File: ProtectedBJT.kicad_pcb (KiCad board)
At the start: 2 copper layers, 38.6 x 40.1 mm, 37 parts, among them P1 CONN_01X04, Q1 BC856, Q2 BC850, Q3 BC856, Q4 BC850, Q5 BC856, Q6 BC850, Q7 BD237, Q8 BD250A

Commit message: some changes on board
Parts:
- moved R10 1.87 mm to (137.2, 113.3)
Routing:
- net Net-(C2-Pad1): track 21.6 -> 24.6 mm
- net GND: track 56.6 -> 58.7 mm
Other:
- board text added: "08/2017 - Protected BJT - V. 0.2 Stefan Helmert - entroserv.de"
- board text removed: "08/2017 - Protected BJT - V. 0.1 Stefan Helmert - entroserv.de"
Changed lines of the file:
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@@
   (general
     (links 54)
-    (no_connects 1)
+    (no_connects 0)
     (area 122.104999 96.21 175.513 144.347001)
     (thickness 1.6)
     (drawings 7)
-    (tracks 200)
+    (tracks 205)
     (zones 0)
     (modules 37)
@@
   )
   (module Resistors_SMD:R_1206 (layer F.Cu)
-    (at 138.115 114.935 180)
+    (at 137.234 113.284 180)
     (descr "Resistor SMD 1206, reflow soldering, Vishay (see dcrcw.pdf)")
     (tags "resistor 1206")
@@
     )
   )
-  (gr_text "08/2017 - Protected BJT - V. 0.1\nStefan Helmert - entroserv.de" (at 144.272 134.62) (layer B.SilkS)
+  (gr_text "08/2017 - Protected BJT - V. 0.2\nStefan Helmert - entroserv.de" (at 144.272 134.62) (layer B.SilkS)
     (effects (font (size 1 1) (thickness 0.2)) (justify mirror))
   )
@@
   (segment (start 148.59 138.31024) (end 148.59 136.96988) (width 0.5) (layer F.Cu) (net 11))
   (segment (start 149.03488 136.525) (end 150.18512 136.525) (width 0.5) (layer F.Cu) (net 11))
+  (segment (start 139.065 116.332) (end 139.065 124.06973) (width 0.5) (layer F.Cu) (net 12))
+  (segment (start 140.335 114.935) (end 139.485 114.935) (width 0.5) (layer F.Cu) (net 12))
+  (segment (start 139.485 114.935) (end 139.065 115.355) (width 0.5) (layer F.Cu) (net 12))
+  (segment (start 139.065 115.355) (end 139.065 116.332) (width 0.5) (layer F.Cu) (net 12))
+  (segment (start 140.335 114.935) (end 138.684 113.284) (width 0.5) (layer F.Cu) (net 12))
   (segment (start 146.05 124.46) (end 146.05 125.735) (width 0.5) (layer F.Cu) (net 12))
   (segment (start 146.05 125.735) (end 142.88 125.735) (width 0.5) (layer F.Cu) (net 12))
@@
   (segment (start 146.685 136.525) (end 146.685 135.25) (width 0.5) (layer F.Cu) (net 12))
   (segment (start 146.685 135.25) (end 146.05 134.615) (width 0.5) (layer F.Cu) (net 12))
-  (segment (start 139.065 114.935) (end 139.065 124.06973) (width 0.5) (layer F.Cu) (net 12))
   (segment (start 139.065 124.06973) (end 139.45527 124.46) (width 0.5) (layer F.Cu) (net 12))
   (segment (start 139.45527 124.46) (end 141.605 124.46) (width 0.5) (layer F.Cu) (net 12))
-  (segment (start 140.335 114.935) (end 139.065 114.935) (width 0.5) (layer F.Cu) (net 12))
   (segment (start 140.97 123.825) (end 141.605 124.46) (width 0.5) (layer F.Cu) (net 12))
   (segment (start 141.605 124.46) (end 139.7 124.46) (width 0.5) (layer F.Cu) (net 12))
@@
   (segment (start 153.67 133.985) (end 151.86 133.985) (width 0.5) (layer F.Cu) (net 18))
   (segment (start 151.86 133.985) (end 151.765 134.08) (width 0.5) (layer F.Cu) (net 18))
+  (segment (start 135.784 113.284) (end 134.14794 113.284) (width 0.5) (layer F.Cu) (net 19))
+  (segment (start 134.14794 113.284) (end 133.35 114.08194) (width 0.5) (layer F.Cu) (net 19))
+  (segment (start 133.35 114.08194) (end 133.35 116.332) (width 0.5) (layer F.Cu) (net 19))
   (segment (start 133.35 116.332) (end 135.768 116.332) (width 0.5) (layer F.Cu) (net 19))
-  (segment (start 135.768 116.332) (end 137.165 114.935) (width 0.5) (layer F.Cu) (net 19))
   (segment (start 132.34924 116.332) (end 133.35 116.332) (width 0.5) (layer F.Cu) (net 19))
   (segment (start 134.372 116.332) (end 133.35 116.332) (width 0.5) (layer F.Cu) (net 19))

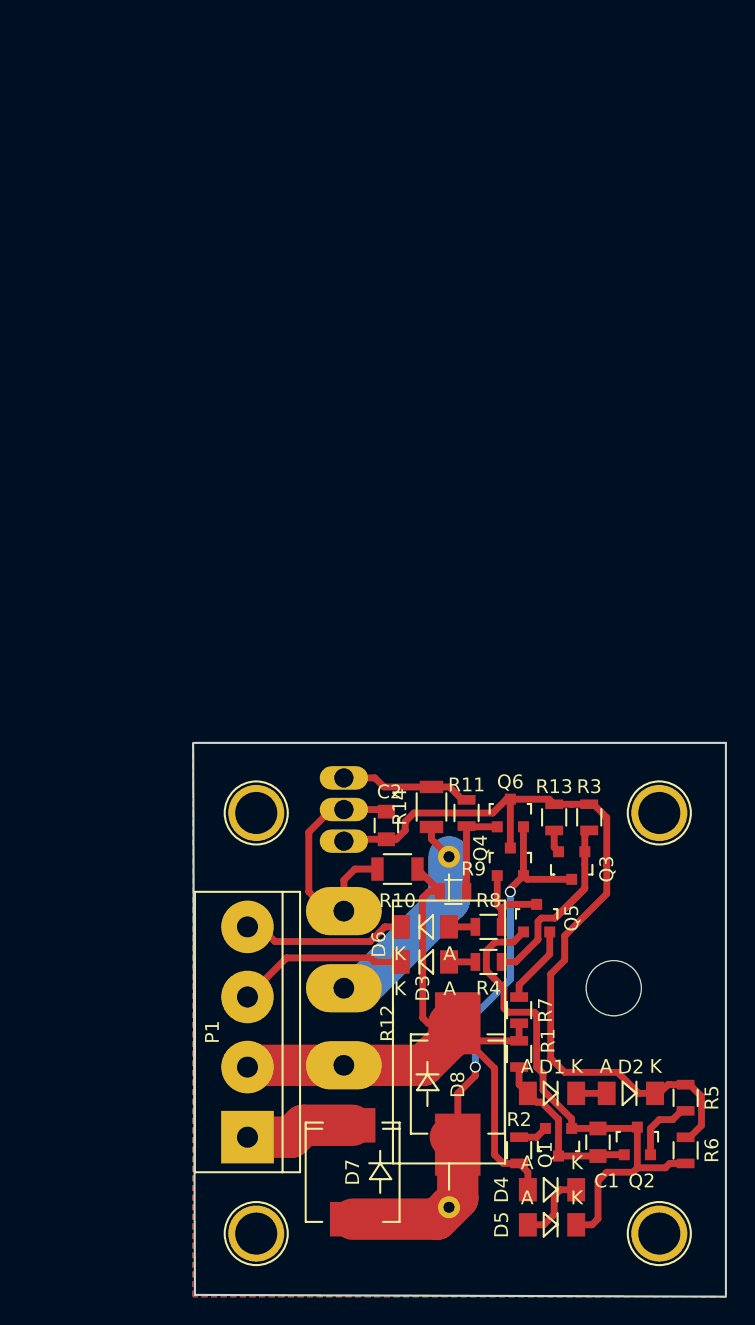
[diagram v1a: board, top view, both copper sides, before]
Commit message: completely new version wth darlington output transistor
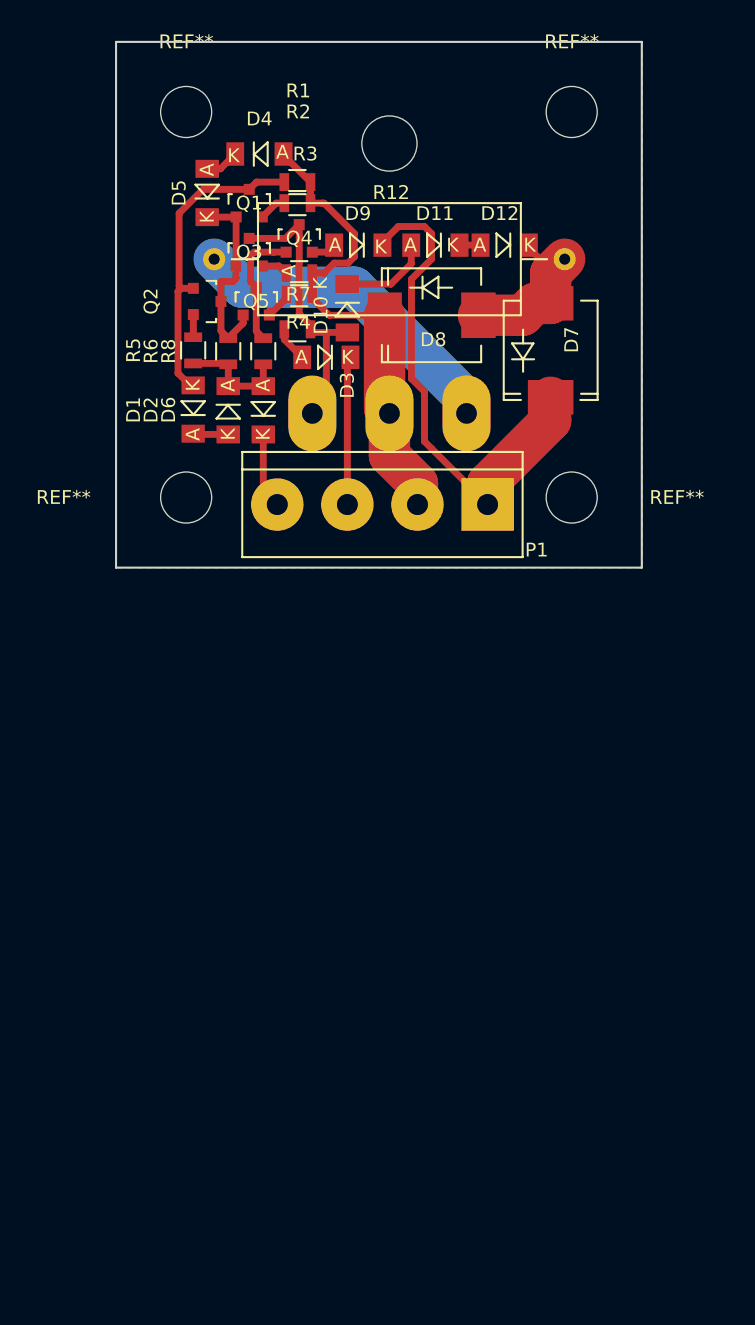
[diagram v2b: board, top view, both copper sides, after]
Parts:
- removed C1, C2: 1p, Capacitors_SMD:C_0805
- removed Q7: BD237, TO_SOT_Packages_THT:SOT126_SOT32_Housing_Vertical_BigPads
- removed Q8: BD250A, TO_SOT_Packages_THT:TO-247_Horizontal_Neutral123_Reverse_largePads
- removed R10: 100, Resistors_SMD:R_1206
- removed R11: 10k, Resistors_SMD:R_0805
- removed R13: 470, Resistors_SMD:R_0805
- removed R14: 2, Resistors_SMD:R_1206
- removed R9: 1M, Resistors_SMD:R_0805
- removed the REF** at (156.2, 139.7)
- removed the REF** at (156.2, 109.2)
- removed the REF** at (127.0, 139.7)
- removed the REF** at (127.0, 109.2)
- added D10: 1N4148, Diodes_SMD:MiniMELF_Standard, F.Cu at (133.6, 72.6)
- added D11: 1N4148, Diodes_SMD:MiniMELF_Standard, F.Cu at (140.0, 68.1)
- added D12: 1N4148, Diodes_SMD:MiniMELF_Standard, F.Cu at (145.0, 68.1)
- added D9: 1N4148, Diodes_SMD:MiniMELF_Standard, F.Cu at (134.4, 68.1)
- added REF**: MountingHole_3-7mm, Mounting_Holes:MountingHole_3-7mm, F.Cu at (121.9, 58.4)
- added REF**: MountingHole_3-7mm, Mounting_Holes:MountingHole_3-7mm, F.Cu at (149.9, 58.4)
- added REF**: MountingHole_3-7mm, Mounting_Holes:MountingHole_3-7mm, F.Cu at (121.9, 86.4)
- added REF**: MountingHole_3-7mm, Mounting_Holes:MountingHole_3-7mm, F.Cu at (149.9, 86.4)
- D8: footprint Diodes_SMD:SMC_Handsoldering -> Diodes_SMD:SMC_Standard
- Q6: value BC850 -> TIP141; footprint TO_SOT_Packages_SMD:SOT-23 -> TO_SOT_Packages_THT:TO-247_Horizontal_Neutral123_Reverse_largePads; moved to B.Cu
- R3: value 1k -> 47
- R4: value 470 -> 47
- R7, R8: value 10k -> 100
- moved D5 78.8 mm to (123.4, 64.3), turned to 90 degrees
- moved D4 78.0 mm to (127.2, 61.5), turned to 0 degrees
- moved Q1 71.7 mm to (126.5, 65.0), turned to 0 degrees
- moved R2 70.5 mm to (130.0, 65.0), turned to 180 degrees
- moved Q2 68.4 mm to (123.4, 72.2), turned to 270 degrees
- moved R6 66.7 mm to (125.0, 75.8), turned to 270 degrees
- moved R1 65.2 mm to (130.0, 63.5), turned to 180 degrees
- moved R5 64.9 mm to (122.4, 75.7), turned to 270 degrees
- moved D7 61.3 mm to (148.3, 75.7), turned to 90 degrees
- moved D2 57.5 mm to (125.0, 80.0), turned to 270 degrees
- moved R12 56.2 mm to (136.7, 69.1), turned to 0 degrees
- moved D1 56.0 mm to (122.4, 80.0), turned to 90 degrees
- moved D8 55.7 mm to (139.7, 73.2), turned to 0 degrees
- moved R7 54.3 mm to (130.1, 71.6), turned to 180 degrees
- moved Q3 50.2 mm to (126.5, 68.6), turned to 0 degrees
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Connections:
- D2 pad 1: Net-(C2-Pad2) -> Net-(D2-Pad1)
- D4 pad 2: GND -> Net-(D4-Pad2)
- D5 pad 1: Net-(C1-Pad1) -> Net-(D5-Pad1)
- D6 pad 1: Net-(D6-Pad1) -> GND
- D6 pad 2: Net-(D6-Pad2) -> Net-(D2-Pad1)
- D7 pad 2: Net-(D7-Pad2) -> Net-(D12-Pad1)
- D8 pad 1: GND -> Net-(D4-Pad2)
- D8 pad 2: Net-(D7-Pad2) -> Net-(D12-Pad1)
- P1 pad 2: GND -> Net-(D4-Pad2)
- P1 pad 4: Net-(D6-Pad1) -> GND
- Q1 pad 1: Net-(C1-Pad1) -> Net-(D5-Pad1)
- Q2 pad 3: Net-(C1-Pad1) -> Net-(D5-Pad1)
- Q3 pad 1: Net-(Q3-Pad1) -> Net-(D5-Pad1)
- Q3 pad 3: Net-(D7-Pad2) -> Net-(D10-Pad2)
- Q4 pad 2: Net-(D7-Pad2) -> Net-(D9-Pad2)
- Q4 pad 3: Net-(C2-Pad2) -> Net-(D10-Pad2)
- Q5 pad 1: Net-(C1-Pad1) -> Net-(D5-Pad1)
- Q6 pad 1: Net-(Q6-Pad1) -> Net-(D10-Pad2)
- Q6 pad 2: Net-(D7-Pad2) -> Net-(D4-Pad2)
- Q6 pad 3: Net-(C2-Pad2) -> Net-(Q6-Pad3)
- R1 pad 1: GND -> Net-(D4-Pad2)
- R12 pad 1: Net-(Q8-Pad2) -> Net-(Q6-Pad3)
- R12 pad 2: Net-(D7-Pad2) -> Net-(D12-Pad1)
- R2 pad 1: GND -> Net-(D4-Pad2)
- R3 pad 1: Net-(C2-Pad2) -> Net-(D4-Pad2)
- R3 pad 2: Net-(Q3-Pad1) -> Net-(Q3-Pad2)
- R4 pad 1: Net-(Q3-Pad1) -> Net-(D10-Pad2)
- R5 pad 2: Net-(C2-Pad2) -> Net-(D2-Pad1)
- R6 pad 1: Net-(C1-Pad1) -> Net-(D5-Pad1)
- R6 pad 2: Net-(C2-Pad2) -> Net-(D2-Pad1)
- R7 pad 1: GND -> Net-(D4-Pad2)
- R8 pad 2: Net-(D6-Pad2) -> Net-(D2-Pad1)
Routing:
- net Net-(C2-Pad2): track 61.6 -> 0.00 mm
- net GND: track 58.7 -> 5.50 mm
- net (no net): track 43.2 -> 0.00 mm
- net Net-(D7-Pad2): track 41.5 -> 0.00 mm, vias 2 -> 0
- net Net-(C1-Pad1): track 39.2 -> 0.00 mm
- net Net-(D4-Pad2): track 0.00 -> 36.0 mm
- net Net-(D7-Pad1): track 7.98 -> 36.6 mm
- net Net-(C2-Pad1): track 24.6 -> 0.00 mm
- net Net-(Q6-Pad3): track 0.00 -> 23.5 mm
- net Net-(D10-Pad2): track 0.00 -> 22.9 mm
- net Net-(Q3-Pad1): track 16.4 -> 0.00 mm
- net Net-(Q8-Pad2): track 16.2 -> 0.00 mm
- net Net-(D5-Pad1): track 0.00 -> 14.5 mm
- net Net-(D12-Pad1): track 0.00 -> 12.9 mm
- net Net-(D6-Pad1): track 12.0 -> 0.00 mm
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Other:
- board size 38.6 x 40.1 mm -> 38.1 x 38.1 mm
- board text removed: "08/2017 - Protected BJT - V. 0.2 Stefan Helmert - entroserv.de"

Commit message: silk screen ready
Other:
- board text added: "B"
- board text added: "C"
- board text added: "E"
- board text added: "Protected Darl. BJT - V. 0.13 (C) 09/2017 Stefan Helmert entroserv.de"
- board text added: "T"
- board text added: "[ ] NPN [ ] PNP"
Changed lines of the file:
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@@
     (area 116.764999 53.264999 155.015001 91.515001)
     (thickness 1.6)
-    (drawings 6)
+    (drawings 18)
     (tracks 123)
     (zones 0)
@@
     (descr "Mounting hole, Befestigungsbohrung, 3,7mm, No Annular, Kein Restring,")
     (tags "Mounting hole, Befestigungsbohrung, 3,7mm, No Annular, Kein Restring,")
-    (fp_text reference REF** (at 0 -5.08) (layer F.SilkS)
+    (fp_text reference REF** (at -7.366 0.254) (layer F.SilkS)
       (effects (font (size 1 1) (thickness 0.15)))
     )
@@
     (descr "Mounting hole, Befestigungsbohrung, 3,7mm, No Annular, Kein Restring,")
     (tags "Mounting hole, Befestigungsbohrung, 3,7mm, No Annular, Kein Restring,")
-    (fp_text reference REF** (at 0 -5.08) (layer F.SilkS)
+    (fp_text reference REF** (at 6.985 0) (layer F.SilkS)
       (effects (font (size 1 1) (thickness 0.15)))
     )
@@
     (descr "Mounting hole, Befestigungsbohrung, 3,7mm, No Annular, Kein Restring,")
     (tags "Mounting hole, Befestigungsbohrung, 3,7mm, No Annular, Kein Restring,")
-    (fp_text reference REF** (at -8.89 0) (layer F.SilkS)
+    (fp_text reference REF** (at -7.112 0.127) (layer F.SilkS)
       (effects (font (size 1 1) (thickness 0.15)))
     )
@@
     (descr "Bornier d'alimentation 4 pins")
     (tags DEV)
-    (fp_text reference P1 (at -11.176 -3.302 180) (layer F.SilkS)
+    (fp_text reference P1 (at -9.271 4.445 180) (layer F.SilkS)
       (effects (font (size 1 1) (thickness 0.15)))
     )
@@
     (tags "Diode Mini-MELF Standard")
     (attr smd)
-    (fp_text reference D3 (at -1.524 -2.032 270) (layer F.SilkS)
+    (fp_text reference D3 (at 0 13.97 360) (layer F.SilkS)
       (effects (font (size 1 1) (thickness 0.15)))
     )
@@
     (tags "Diode Mini-MELF Standard")
     (attr smd)
-    (fp_text reference D4 (at 0 -2.54) (layer F.SilkS)
+    (fp_text reference D4 (at 0.02794 -6.223) (layer F.SilkS)
       (effects (font (size 1 1) (thickness 0.15)))
     )
@@
     (tags "Diode SMC Standard")
     (attr smd)
-    (fp_text reference D7 (at 0.762 1.524 90) (layer F.SilkS)
+    (fp_text reference D7 (at 0.127 4.191 90) (layer F.SilkS)
       (effects (font (size 1 1) (thickness 0.15)))
     )
@@
     (tags "Diode Mini-MELF Standard")
     (attr smd)
-    (fp_text reference D10 (at 0.508 1.905 450) (layer F.SilkS)
+    (fp_text reference D10 (at -0.381 12.446 450) (layer F.SilkS)
       (effects (font (size 1 1) (thickness 0.15)))
     )
@@
     (fp_line (start 0.60052 0.85) (end -0.40024 0) (layer F.SilkS) (width 0.15))
     (fp_line (start -0.40024 -0.85) (end -0.40024 0.85) (layer F.SilkS) (width 0.15))
-    (fp_text user K (at -1.8 1.95 270) (layer F.SilkS)
-      (effects (font (size 1 1) (thickness 0.15)))
-    )
-    (fp_text user A (at -2.7051 4.2164 270) (layer F.SilkS)
+    (fp_text user K (at -1.905 0 270) (layer F.SilkS)
+      (effects (font (size 1 1) (thickness 0.15)))
+    )
+    (fp_text user A (at 1.651 0 270) (layer F.SilkS)
       (effects (font (size 1 1) (thickness 0.15)))
     )
@@
     (fp_line (start 0.60052 0.85) (end -0.40024 0) (layer F.SilkS) (width 0.15))
     (fp_line (start -0.40024 -0.85) (end -0.40024 0.85) (layer F.SilkS) (width 0.15))
-    (fp_text user K (at -1.24206 0 180) (layer F.SilkS)
+    (fp_text user K (at -1.87706 0 180) (layer F.SilkS)
       (effects (font (size 1 1) (thickness 0.15)))
     )
@@
     (tags SOT-23)
     (attr smd)
-    (fp_text reference Q1 (at 0 0) (layer F.SilkS)
+    (fp_text reference Q1 (at -0.254 -8.382) (layer F.SilkS)
       (effects (font (size 1 1) (thickness 0.15)))
     )
@@
     (tags SOT-23)
     (attr smd)
-    (fp_text reference Q3 (at 0 0) (layer F.SilkS)
+    (fp_text reference Q3 (at -0.381 -10.541) (layer F.SilkS)
       (effects (font (size 1 1) (thickness 0.15)))
     )
@@
     (tags SOT-23)
     (attr smd)
-    (fp_text reference Q4 (at 0 -0.01524) (layer F.SilkS)
+    (fp_text reference Q4 (at -0.32 -10.30224) (layer F.SilkS)
       (effects (font (size 1 1) (thickness 0.15)))
     )
@@
     (tags SOT-23)
     (attr smd)
-    (fp_text reference Q5 (at 0 0) (layer F.SilkS)
+    (fp_text reference Q5 (at -0.127 -12.573) (layer F.SilkS)
       (effects (font (size 1 1) (thickness 0.15)))
     )
@@
     (tags "resistor 0805")
     (attr smd)
-    (fp_text reference R1 (at -0.066 6.604 180) (layer F.SilkS)
+    (fp_text reference R1 (at 0.188 8.763 360) (layer F.SilkS)
       (effects (font (size 1 1) (thickness 0.15)))
     )
@@
     (tags "resistor 0805")
     (attr smd)
-    (fp_text reference R2 (at -0.066 6.604 180) (layer F.SilkS)
+    (fp_text reference R2 (at 0.188 9.017 360) (layer F.SilkS)
       (effects (font (size 1 1) (thickness 0.15)))
     )
@@
     (tags "resistor 0805")
     (attr smd)
-    (fp_text reference R3 (at -0.442 8.636 180) (layer F.SilkS)
+    (fp_text reference R3 (at 0.32 11.557 360) (layer F.SilkS)
       (effects (font (size 1 1) (thickness 0.15)))
     )
@@
     (tags "resistor 0805")
     (attr smd)
-    (fp_text reference R4 (at -0.066 0.508 180) (layer F.SilkS)
+    (fp_text reference R4 (at -0.701 13.081 360) (layer F.SilkS)
       (effects (font (size 1 1) (thickness 0.15)))
     )
@@
     (tags "resistor 0805")
     (attr smd)
-    (fp_text reference R7 (at 0.066 0 180) (layer F.SilkS)
+    (fp_text reference R7 (at 0.32 11.811 360) (layer F.SilkS)
       (effects (font (size 1 1) (thickness 0.15)))
     )
@@
     (tags "Diode SMC Standard")
     (attr smd)
-    (fp_text reference D8 (at 0.127 1.778) (layer F.SilkS)
+    (fp_text reference D8 (at -0.127 4.064) (layer F.SilkS)
       (effects (font (size 1 1) (thickness 0.15)))
     )
@@
     (descr "Mounting hole, Befestigungsbohrung, 3,7mm, No Annular, Kein Restring,")
     (tags "Mounting hole, Befestigungsbohrung, 3,7mm, No Annular, Kein Restring,")
-    (fp_text reference REF** (at 7.62 0) (layer F.SilkS)
+    (fp_text reference REF** (at 6.858 0.508) (layer F.SilkS)
       (effects (font (size 1 1) (thickness 0.15)))
     )
@@
     (pad 1 thru_hole circle (at 0 0) (size 3.7 3.7) (drill 3.7) (layers))
   )
+  (gr_text "[ ] NPN\n[ ] PNP" (at 143.51 61.976) (layer F.SilkS)
+    (effects (font (size 1.5 1.5) (thickness 0.3)))
+  )
+  (gr_text "[ ] NPN\n[ ] PNP" (at 149.606 73.66) (layer B.SilkS)
+    (effects (font (size 1.5 1.5) (thickness 0.3)) (justify mirror))
+  )
+  (gr_text "Protected Darl. BJT - V. 0.13\n(C) 09/2017 Stefan Helmert\n    entroserv.de" (at 119.888 61.849 90) (layer B.SilkS)
+    (effects (font (size 0.75 0.75) (thickness 0.15)) (justify left mirror))
+  )
+  (gr_text "Protected Darl. BJT - V. 0.13\n(C) 09/2017 Stefan Helmert\n    entroserv.de" (at 131.191 56.007) (layer F.SilkS)
+    (effects (font (size 0.75 0.75) (thickness 0.15)) (justify left))
+  )
+  (gr_text E (at 146.939 89.662) (layer B.SilkS)
+    (effects (font (size 1.5 1.5) (thickness 0.3)) (justify mirror))
+  )
+  (gr_text C (at 140.716 89.789) (layer B.SilkS)
+    (effects (font (size 1.5 1.5) (thickness 0.3)) (justify mirror))
+  )
+  (gr_text B (at 135.89 89.662) (layer B.SilkS)
+    (effects (font (size 1.5 1.5) (thickness 0.3)) (justify mirror))
+  )
+  (gr_text T (at 130.937 89.408 180) (layer B.SilkS)
+    (effects (font (size 1.5 1.5) (thickness 0.3)) (justify mirror))
+  )
+  (gr_text E (at 146.939 89.789) (layer F.SilkS)
+    (effects (font (size 1.5 1.5) (thickness 0.3)))
+  )
+  (gr_text C (at 140.589 89.662) (layer F.SilkS)
+    (effects (font (size 1.5 1.5) (thickness 0.3)))
+  )
+  (gr_text "B\n" (at 136.017 89.662) (layer F.SilkS)
+    (effects (font (size 1.5 1.5) (thickness 0.3)))
+  )
+  (gr_text T (at 130.937 89.408 180) (layer F.SilkS)
+    (effects (font (size 1.5 1.5) (thickness 0.3)))
+  )
   (dimension 38.1 (width 0.3) (layer Cmts.User)

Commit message: second produced version
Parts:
- moved R12 0.63 mm to (136.0, 69.1)
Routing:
- net Net-(D1-Pad2): track 22.7 -> 24.0 mm
- net Net-(D12-Pad1): track 12.9 -> 11.5 mm
- net Net-(D4-Pad2): track 36.0 -> 37.1 mm
- net Net-(D7-Pad1): track 36.6 -> 37.6 mm
- net Net-(Q6-Pad3): track 23.5 -> 24.1 mm
- net Net-(D5-Pad1): track 14.5 -> 14.0 mm
